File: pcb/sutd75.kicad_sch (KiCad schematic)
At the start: 44 parts, among them J1 SWD Header, J2 UART header, J3 USB_C_Receptacle_USB2.0, J4 I2C header, SW1 BOOT0, SW2 BOOT1, SW3 RESET, U1 XC6206PxxxMR, U2 STM32F103RBTx, U3 USBLC6-2SC6

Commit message: Update schematic and BOM with new AlpsAlpine part
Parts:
- SW1, SW2: footprint large-arisu:SW_SPDTx01_SMD_AlpsAlpine-SSSS811101 -> large-arisu:SW_SPDTx01_SMD_AlpsAlpine-SSSS710607; LSCS C109335 -> C160876
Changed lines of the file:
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@@
     (property "Reference" "SW2" (id 0) (at 35.56 62.23 0))
     (property "Value" "BOOT1" (id 1) (at 35.56 59.9186 0))
-    (property "Footprint" "large-arisu:SW_SPDTx01_SMD_AlpsAlpine-SSSS811101" (id 2) (at 35.56 53.975 0)
+    (property "Footprint" "large-arisu:SW_SPDTx01_SMD_AlpsAlpine-SSSS710607" (id 2) (at 35.56 53.975 0)
       (effects (font (size 1.27 1.27)) hide)
     )
@@
       (effects (font (size 1.27 1.27)) hide)
     )
-    (property "LSCS" "C109335" (id 4) (at 35.56 53.975 0)
+    (property "LSCS" "C160876" (id 4) (at 35.56 53.975 0)
       (effects (font (size 1.27 1.27)) hide)
     )
@@
     (property "Reference" "SW1" (id 0) (at 35.56 35.306 0))
     (property "Value" "BOOT0" (id 1) (at 35.56 37.6174 0))
-    (property "Footprint" "large-arisu:SW_SPDTx01_SMD_AlpsAlpine-SSSS811101" (id 2) (at 35.56 42.545 0)
+    (property "Footprint" "large-arisu:SW_SPDTx01_SMD_AlpsAlpine-SSSS710607" (id 2) (at 35.56 42.545 0)
       (effects (font (size 1.27 1.27)) hide)
     )
@@
       (effects (font (size 1.27 1.27)) hide)
     )
-    (property "LSCS" "C109335" (id 4) (at 35.56 42.545 0)
+    (property "LSCS" "C160876" (id 4) (at 35.56 42.545 0)
       (effects (font (size 1.27 1.27)) hide)
     )
@@
     )
     (path "/ed388f6e-fac3-41c0-883a-ab9353f949b2"
-      (reference "SW1") (unit 1) (value "BOOT0") (footprint "large-arisu:SW_SPDTx01_SMD_AlpsAlpine-SSSS811101")
+      (reference "SW1") (unit 1) (value "BOOT0") (footprint "large-arisu:SW_SPDTx01_SMD_AlpsAlpine-SSSS710607")
     )
     (path "/aaf47ffd-208b-41d2-8ff3-ae17563fd34f"
-      (reference "SW2") (unit 1) (value "BOOT1") (footprint "large-arisu:SW_SPDTx01_SMD_AlpsAlpine-SSSS811101")
+      (reference "SW2") (unit 1) (value "BOOT1") (footprint "large-arisu:SW_SPDTx01_SMD_AlpsAlpine-SSSS710607")
     )
     (path "/30ff18db-76db-4e28-8310-c7909df52ea7"

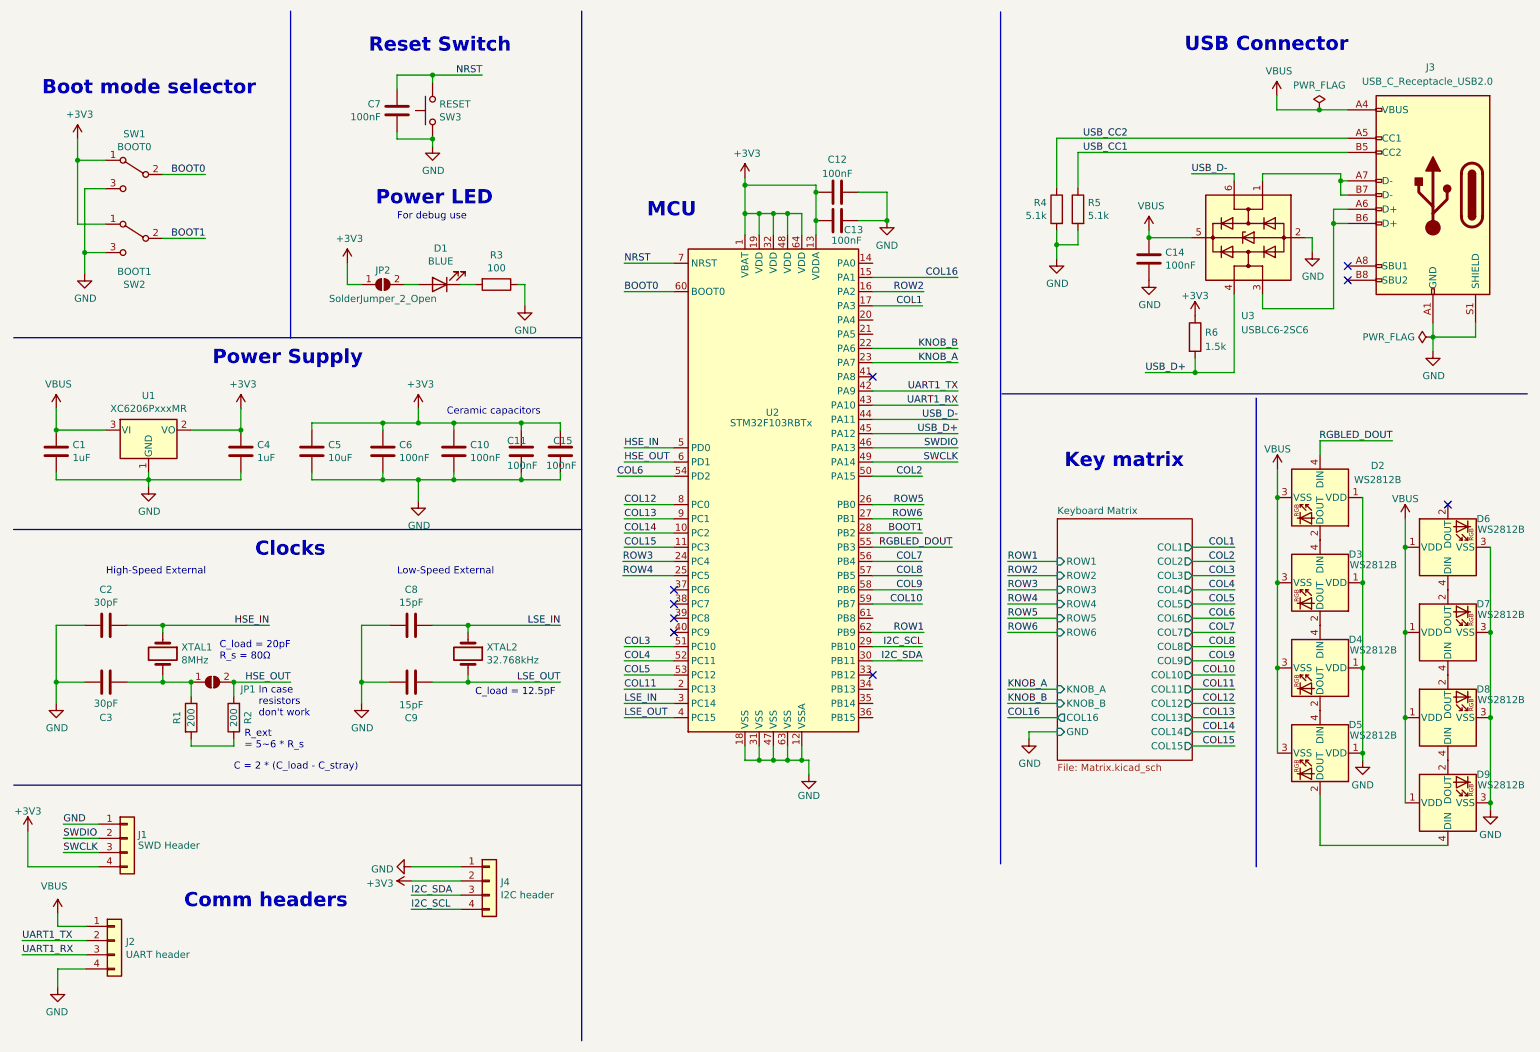
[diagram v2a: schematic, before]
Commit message: Add breakout pin header for unused pins on MCU
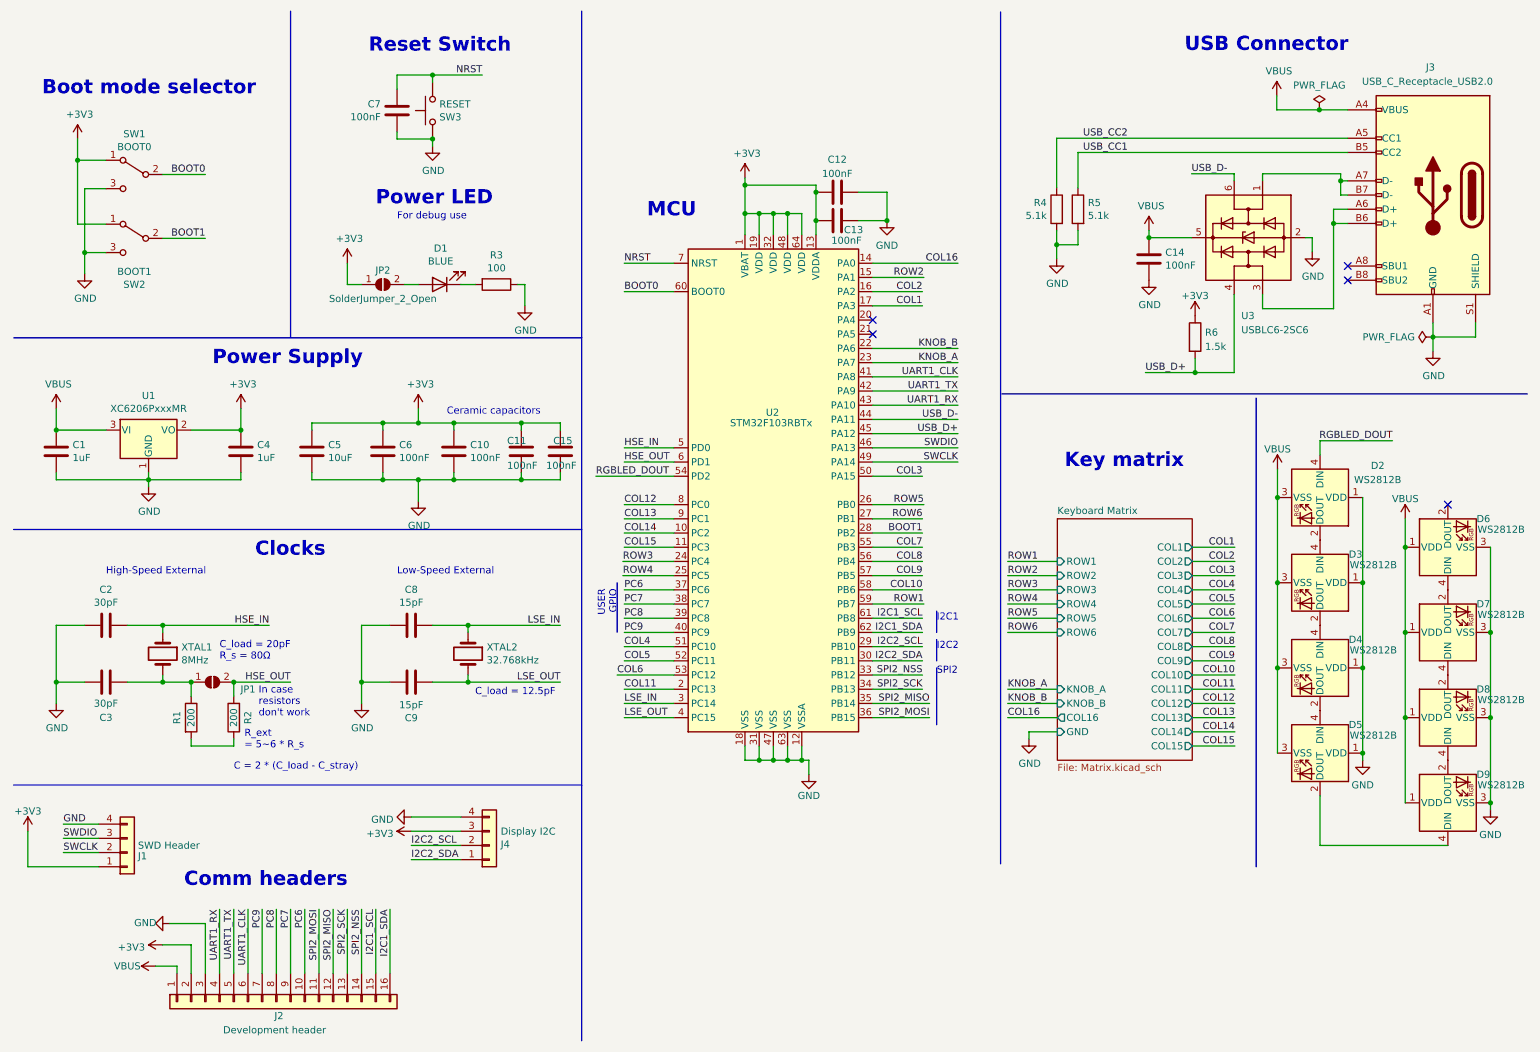
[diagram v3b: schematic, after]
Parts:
- J2: value UART header -> Development header; footprint Connector_PinHeader_2.54mm:PinHeader_1x04_P2.54mm_Vertical -> Connector_PinHeader_2.54mm:PinHeader_1x16_P2.54mm_Vertical; symbol Connector_Generic:Conn_01x04 -> Connector_Generic:Conn_01x16
- J4: value I2C header -> Display I2C
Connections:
- net +3V3: now also J1.1 (Pin_1), J2.2 (Pin_2), J4.3 (Pin_3); no longer J1.4 (Pin_4), J4.2 (Pin_2)
- net COL10: now also U2.58 (PB6); no longer U2.59 (PB7)
- net COL16: now also U2.14 (PA0); no longer U2.15 (PA1)
- net COL2: now also U2.16 (PA2); no longer U2.50 (PA15)
- net COL3: now also U2.50 (PA15); no longer U2.51 (PC10)
- net COL4: now also U2.51 (PC10); no longer U2.52 (PC11)
- net COL5: now also U2.52 (PC11); no longer U2.53 (PC12)
- net COL6: now also U2.53 (PC12); no longer U2.54 (PD2)
- net COL7: now also U2.55 (PB3); no longer U2.56 (PB4)
- net COL8: now also U2.56 (PB4); no longer U2.57 (PB5)
- net COL9: now also U2.57 (PB5); no longer U2.58 (PB6)
- net GND: now also J1.4 (Pin_4), J2.3 (Pin_3), J4.4 (Pin_4); no longer J1.1 (Pin_1), J2.4 (Pin_4), J4.1 (Pin_1)
- net RGBLED_DOUT: now also U2.54 (PD2); no longer U2.55 (PB3)
- net ROW1: now also U2.59 (PB7); no longer U2.62 (PB9)
- net ROW2: now also U2.15 (PA1); no longer U2.16 (PA2)
- net SWCLK: now also J1.2 (Pin_2); no longer J1.3 (Pin_3)
- net SWDIO: now also J1.3 (Pin_3); no longer J1.2 (Pin_2)
- net UART1_RX: now also J2.4 (Pin_4); no longer J2.3 (Pin_3)
- net UART1_TX: now also J2.5 (Pin_5); no longer J2.2 (Pin_2)
- net SPI2_NSS: now reaches U2.33 (PB12)
- net SPI2_NSS: now also J2.14 (Pin_14)
- net SPI2_SCK: now reaches U2.34 (PB13)
- net SPI2_SCK: now also J2.13 (Pin_13)
- net SPI2_MISO: now reaches U2.35 (PB14)
- net SPI2_MISO: now also J2.12 (Pin_12)
- net SPI2_MOSI: now reaches U2.36 (PB15)
- net SPI2_MOSI: now also J2.11 (Pin_11)
- net PC6: now reaches U2.37 (PC6)
- net PC6: now also J2.10 (Pin_10)
- net PC7: now reaches U2.38 (PC7)
- net PC7: now also J2.9 (Pin_9)
- net PC8: now reaches U2.39 (PC8)
- net PC8: now also J2.8 (Pin_8)
- net PC9: now reaches U2.40 (PC9)
- net PC9: now also J2.7 (Pin_7)
- net UART1_CLK: now reaches U2.41 (PA8)
- net UART1_CLK: now also J2.6 (Pin_6)
- net I2C1_SCL: now reaches U2.61 (PB8)
- net I2C1_SCL: now also J2.15 (Pin_15)
- net I2C_SCL renamed I2C2_SCL
- net I2C2_SCL: now also J4.2 (Pin_2); no longer J4.4 (Pin_4)
- net I2C_SDA renamed I2C2_SDA
- net I2C2_SDA: now also J4.1 (Pin_1); no longer J4.3 (Pin_3)
- new net I2C1_SDA: J2.16 (Pin_16), U2.62 (PB9)
- no-connect marks 9 -> 5
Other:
- note added: "I2C1"
- note added: "I2C2"
- note added: "SPI2"
- note added: "USER GPIO"
- moved on the sheet: J4
